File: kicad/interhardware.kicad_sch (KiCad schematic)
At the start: 66 parts, among them J1 RJ11, J2 RJ11, J4 USB_C_Receptacle_USB2.0_14P, Q1 MMBTA42, Q2 MMBTA92, Q3 MMBTA42, Q4 MMBTA06, Q5 MMBTA06, SW1 SW_Omron_B3FS, U4 TPS62162DSG, U5 ESP32-C3-WROOM-02

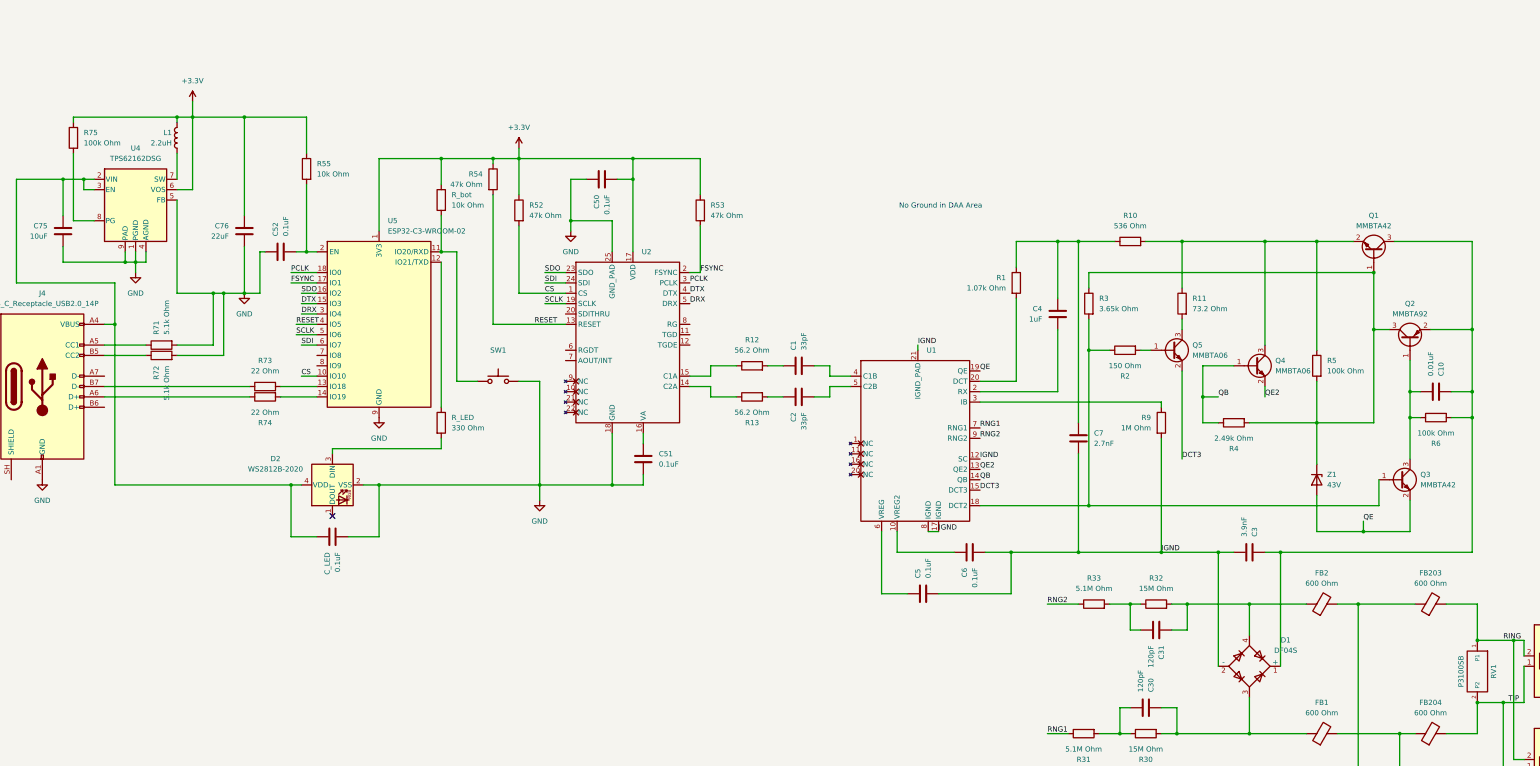
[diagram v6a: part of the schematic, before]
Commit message: todos os footprints
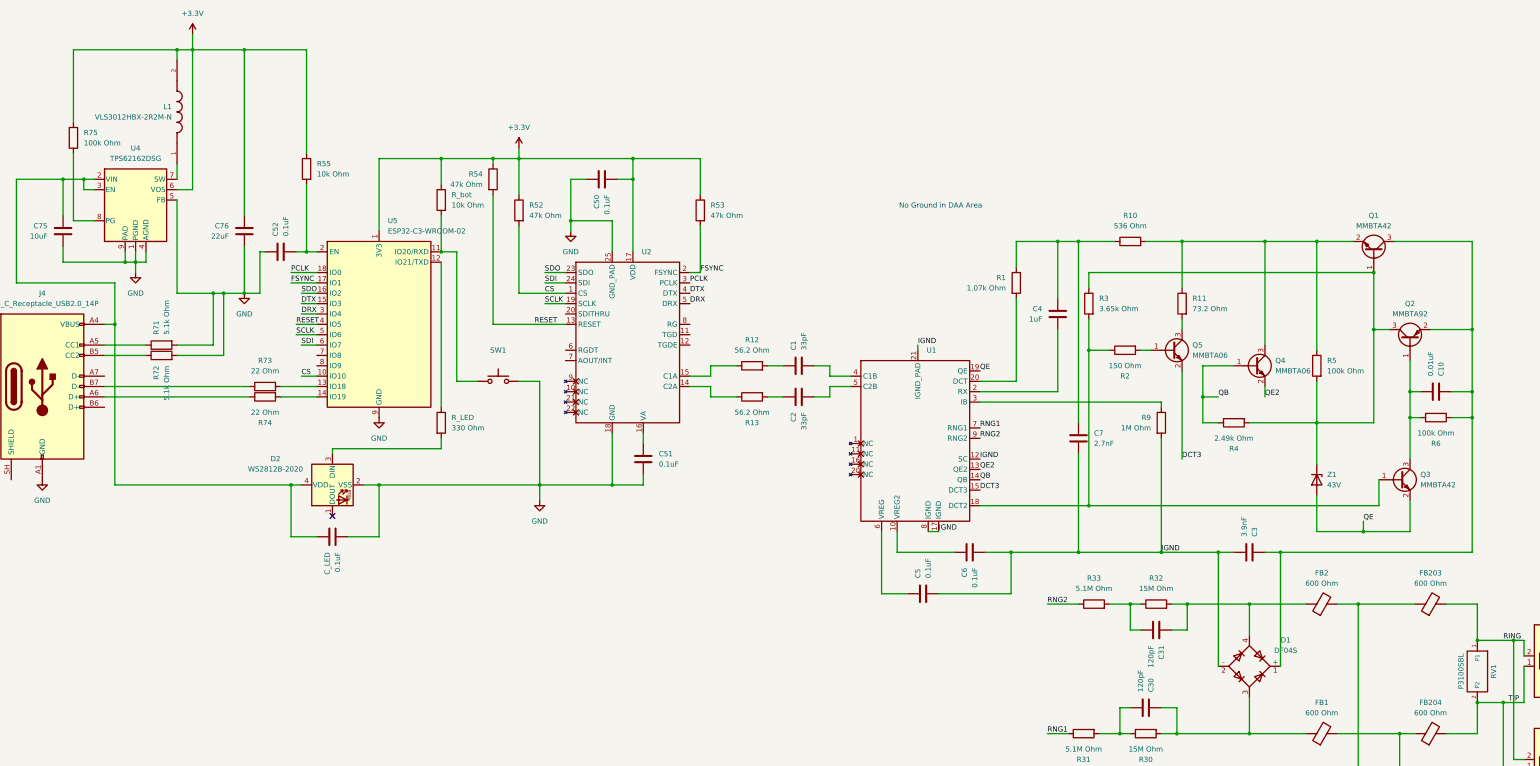
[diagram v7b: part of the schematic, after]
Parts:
- removed L1: 2.2uH, symbol Device:L
- added L1: VLS3012HBX-2R2M-N, VLS3012HBX-2R2M-N:IND_VLS3012HBX-2R2M-N, symbol interbridge_telephony:VLS3012HBX-2R2M-N
- C1, C2, C8, C9: footprint (none) -> Capacitor_SMD:C_1808_4520Metric
- C10, C5, C6, C7: footprint (none) -> Capacitor_SMD:C_0603_1608Metric
- C3, C30, C31: footprint (none) -> Capacitor_SMD:C_1206_3216Metric
- C4: footprint (none) -> Capacitor_SMD:CP_Elec_4x5.4
- C75, C76: footprint (none) -> Capacitor_SMD:C_0805_2012Metric
- FB1, FB2, FB203, FB204: footprint (none) -> Inductor_SMD:L_0603_1608Metric
- R1, R10, R11, R3, R30, R31, R32, R33, R4: footprint (none) -> Resistor_SMD:R_1206_3216Metric
- R12, R13, R2, R5, R6, R9: footprint (none) -> Resistor_SMD:R_0603_1608Metric
- RV1: value P3100SB -> P3100SBL; footprint (none) -> Diode_SMD:D_SMB
- Z1: footprint (none) -> Diode_SMD:D_SOD-123
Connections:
- net +3.3V: now also L1.2
- net at U4.7 (SW): now also L1.1

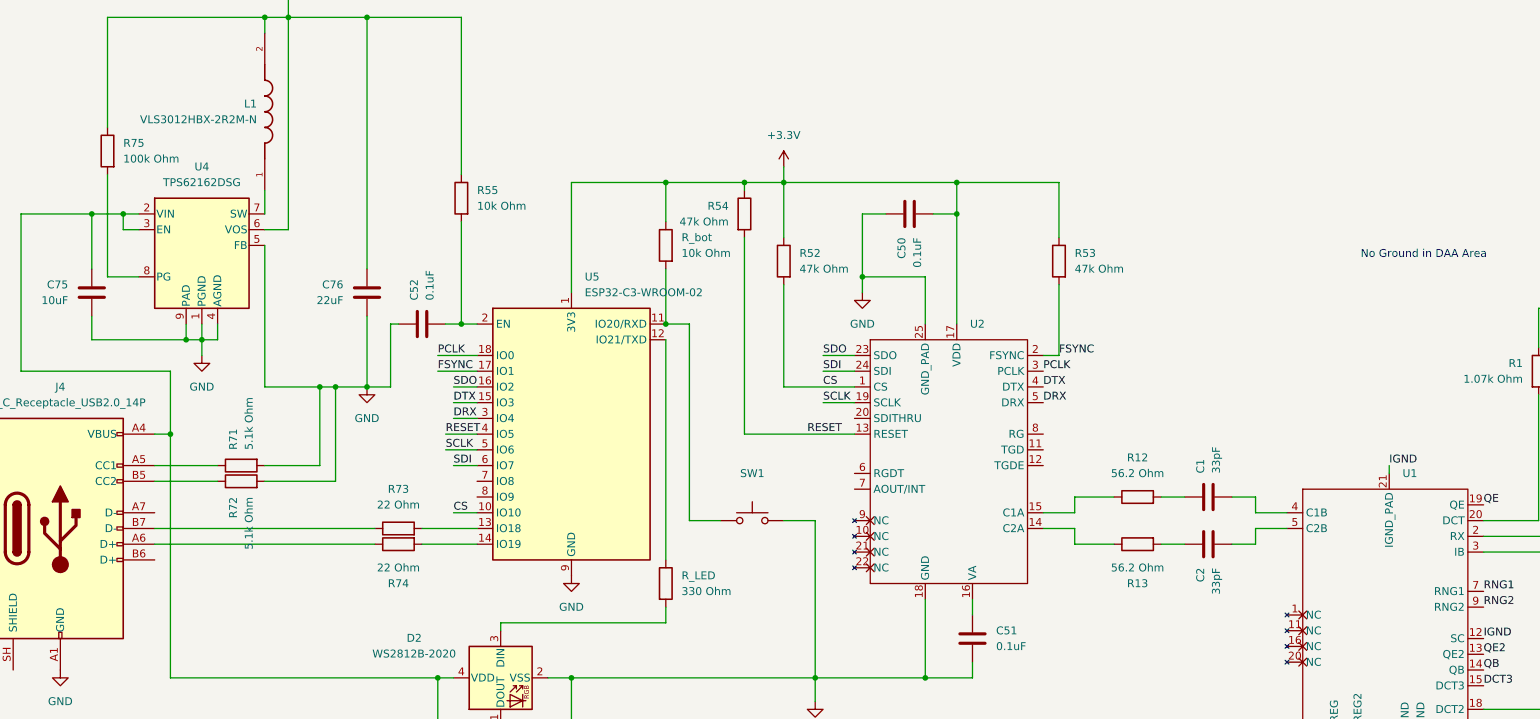
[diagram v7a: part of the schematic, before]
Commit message: audit schematic footprints and component metadata
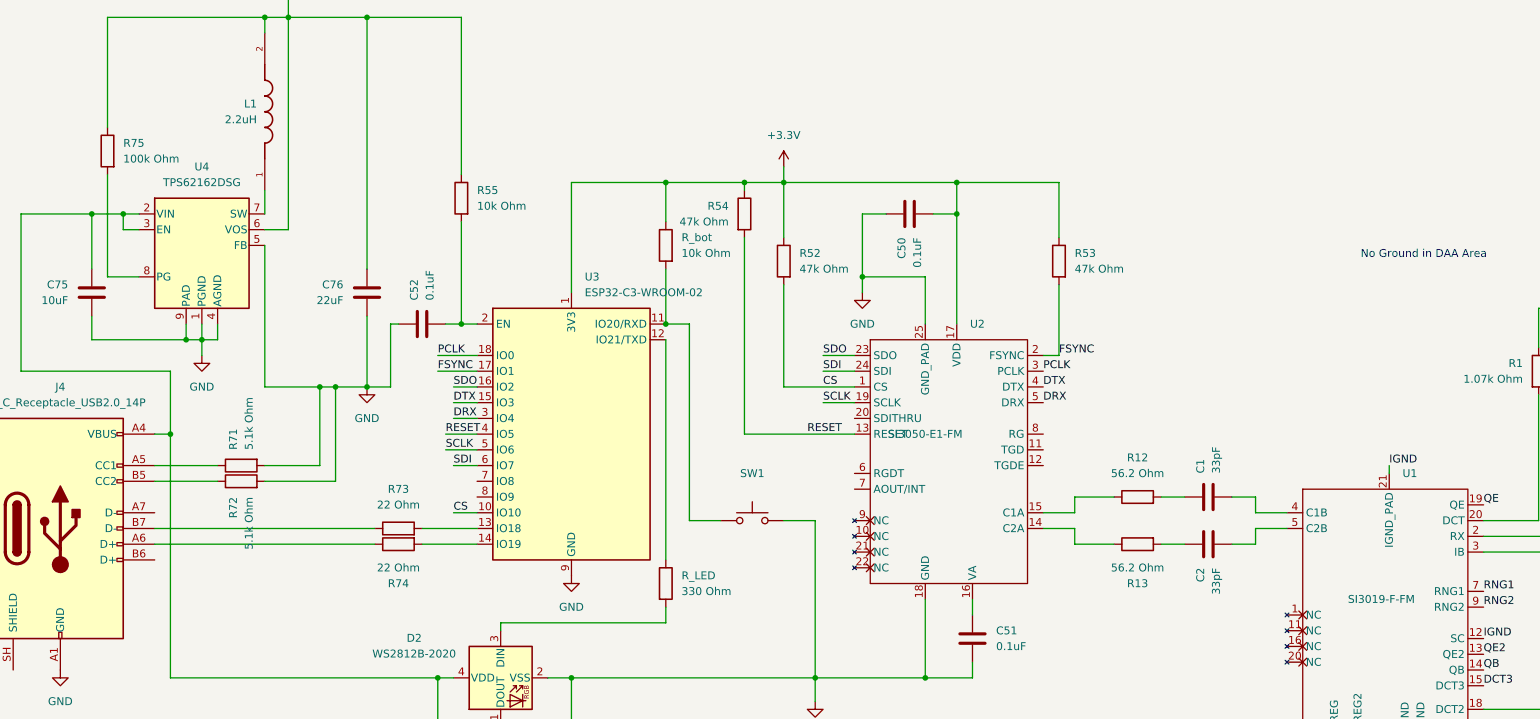
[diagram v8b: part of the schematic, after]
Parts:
- C1, C2: MPN (none) -> GA342A1XGF330JW31L; Manufacturer (none) -> Murata; Package (none) -> 1808 / 4520 metric
- C10, C5, C50, C51, C52, C6, C7, C_LED, R12, R13, R2, R5, R52, R53, R54, R55, R6, R71, R72, R73, R74, R75, R9, R_LED, R_bot: MPN (none) -> GENERIC; Manufacturer (none) -> GENERIC; Package (none) -> 0603_1608Metric
- C3, C30, C31, R1, R10, R11, R3, R30, R31, R32, R33, R4: MPN (none) -> GENERIC; Manufacturer (none) -> GENERIC; Package (none) -> 1206_3216Metric
- C4: MPN (none) -> EEE-1HA010NR; Manufacturer (none) -> Panasonic; Package (none) -> SMD aluminum electrolytic, 4 x 5.4 mm
- C75, C76: MPN (none) -> GENERIC; Manufacturer (none) -> GENERIC; Package (none) -> 0805_2012Metric
- C8, C9: MPN (none) -> GA342QR7GF681KW01L; Manufacturer (none) -> Murata; Package (none) -> 1808 / 4520 metric
- D1, J1, J2, J4, SW1: MPN (none) -> VERIFY; Manufacturer (none) -> VERIFY; Package (none) -> VERIFY
- D2: MPN (none) -> WS2812B-2020; Manufacturer (none) -> Worldsemi; Package (none) -> PLCC-4, 2.0 x 2.0 mm
- FB1, FB2, FB203, FB204: MPN (none) -> BLM18AG601SN1; Manufacturer (none) -> Murata; Package (none) -> 0603 / 1608 metric
- L1: value VLS3012HBX-2R2M-N -> 2.2uH; footprint VLS3012HBX-2R2M-N:IND_VLS3012HBX-2R2M-N -> interbridge_telephony:IND_VLS3012HBX-2R2M-N; MPN (none) -> VLS3012HBX-2R2M-N; Manufacturer (none) -> TDK; Package None -> VLS3012 SMD
- Q1, Q3: MPN (none) -> MMBTA42; Manufacturer (none) -> TBD; Package (none) -> SOT-23
- Q2: MPN (none) -> MMBTA92; Manufacturer (none) -> TBD; Package (none) -> SOT-23
- Q4, Q5: MPN (none) -> MMBTA06; Manufacturer (none) -> TBD; Package (none) -> SOT-23
- RV1: MPN (none) -> P3100SBL; Manufacturer (none) -> Littelfuse; Package (none) -> DO-214AA (SMB)
- U1: value (none) -> SI3019-F-FM; MPN (none) -> SI3019-F-FM; Manufacturer (none) -> Skyworks Solutions; Package (none) -> QFN-20 + exposed IGND pad
- U2: value (none) -> SI3050-E1-FM; MPN (none) -> SI3050-E1-FM; Manufacturer (none) -> Skyworks Solutions; Package (none) -> QFN-24 + exposed GND pad
- U3: renamed from U5; MPN (none) -> ESP32-C3-WROOM-02; Manufacturer (none) -> Espressif Systems; Package (none) -> Module with integrated PCB antenna
- U4: MPN (none) -> TPS62162DSG; Manufacturer (none) -> Texas Instruments; Package (none) -> WSON-8 DSG + exposed pad
- Z1: MPN (none) -> MMSZ43T1G; Manufacturer (none) -> onsemi; Package (none) -> SOD-123
